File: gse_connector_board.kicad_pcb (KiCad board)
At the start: 2 copper layers, 52.2 x 27 mm, 27 parts, among them J1 arming_connector, J2 gse_com_connector, J3 chg_connector, J4 Conn_02x03_Top_Bottom, J5 Conn_02x02_Top_Bottom, U7 ISO1044BD, U9 MCP2562-E-SN

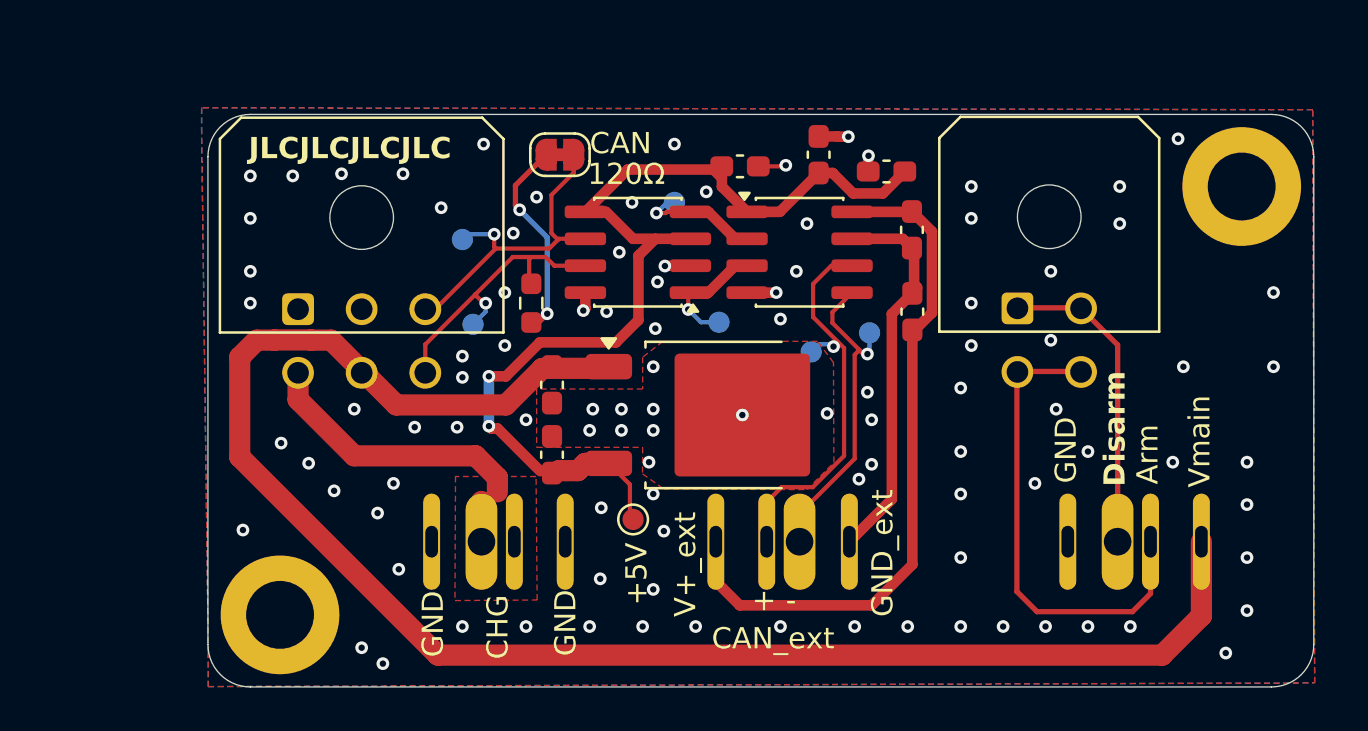
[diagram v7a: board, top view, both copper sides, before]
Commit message: edited grounding and edge cuts
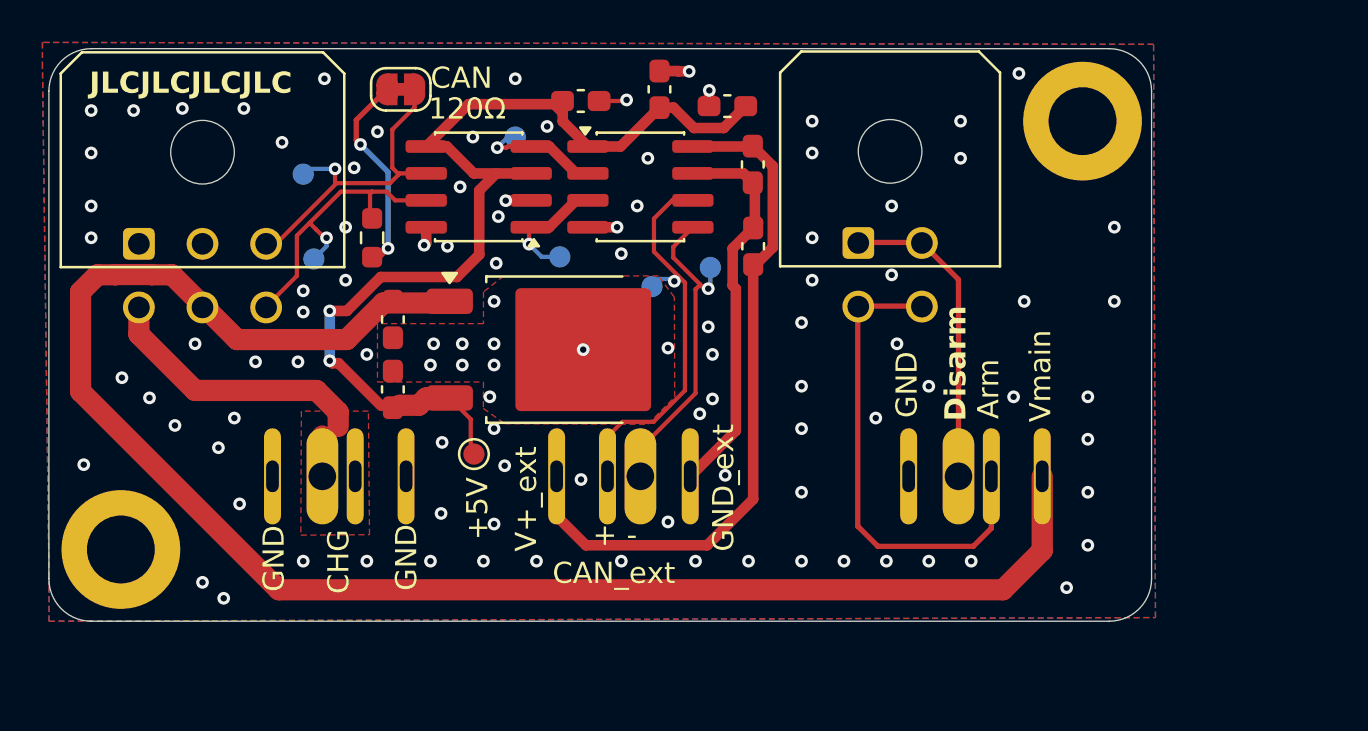
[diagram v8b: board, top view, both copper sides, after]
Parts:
- moved G*** 8.11 mm to (125.4, 56.1)
- moved H2 8.11 mm to (113.4, 76.6)
- moved J3 8.11 mm to (122.9, 76.2)
- moved C19 8.11 mm to (126.2, 69.1)
- moved C23 8.11 mm to (143.2, 62.3)
- moved C24 8.11 mm to (143.2, 58.5)
- moved C28 8.11 mm to (142.0, 55.7)
- moved J1 8.11 mm to (152.9, 76.2)
- moved J2 8.11 mm to (137.9, 70.2)
- moved J5 8.11 mm to (148.2, 62.2)
- moved TP4 8.11 mm to (141.2, 63.3)
- moved TP6 8.11 mm to (134.1, 62.8)
- moved TP7 8.11 mm to (130.0, 72.1)
- moved Ue1 8.11 mm to (133.9, 67.2)
- moved C22 8.11 mm to (135.1, 55.5)
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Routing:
- net CAN_1+: track 13.7 -> 14.5 mm
- net GND: vias 101 -> 104
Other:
- board size 52.2 x 27 mm -> 52 x 27 mm
